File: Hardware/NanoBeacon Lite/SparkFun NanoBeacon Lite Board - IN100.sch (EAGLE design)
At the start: 34 parts, among them J3 Vertical Qwiic Connector, U1 IN100, Y1 CRYSTAL-26MHZSMD-3.2X2.5

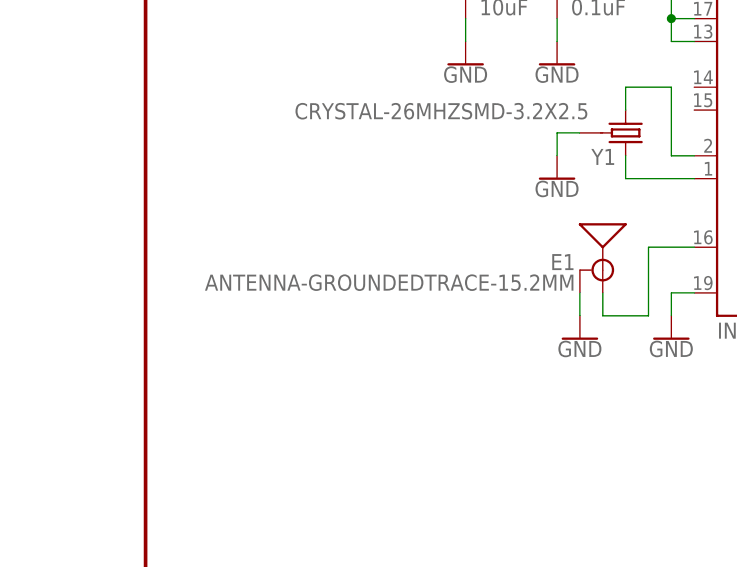
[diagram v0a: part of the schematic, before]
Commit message: Remove library file
Part is in SFE Eagle library, update part in design
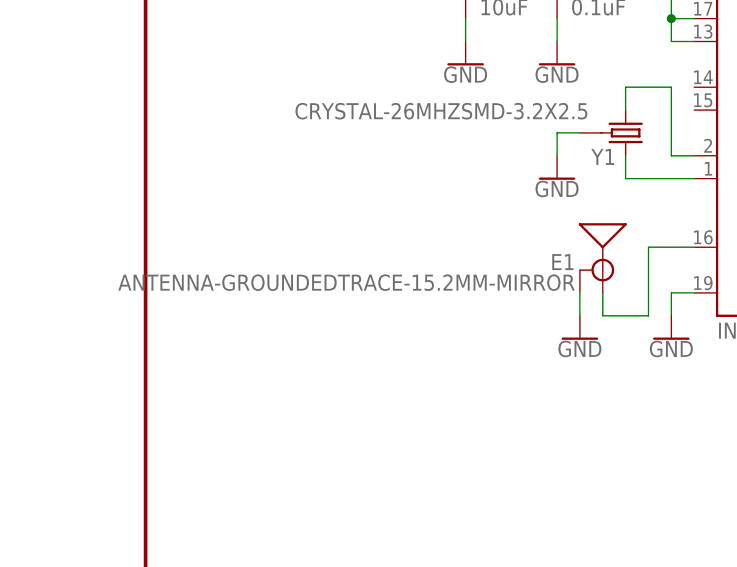
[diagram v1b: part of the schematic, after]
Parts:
- BT1: device SparkFun-Batteries:BATTERY-12MM_SMD -> SparkFun-Batteries:BATTERY-12MM_SMD_BOTH_PWR_PADS
- E1: value ANTENNA-GROUNDEDTRACE-15.2MM -> ANTENNA-GROUNDEDTRACE-15.2MM-MIRROR; device SparkFun-RF:ANTENNA-GROUNDEDTRACE-15.2MM -> SparkFun-RF:ANTENNA-GROUNDEDTRACE-15.2MM-MIRROR
- U1: device IN100:IN100 -> SparkFun-RF:IN100
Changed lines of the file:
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@@
 </classes>
 <parts>
-<part name="E1" library="SparkFun-RF" deviceset="ANTENNA-GROUNDED" device="TRACE-15.2MM"/>
+<part name="E1" library="SparkFun-RF" deviceset="ANTENNA-GROUNDED" device="TRACE-15.2MM-MIRROR" value="ANTENNA-GROUNDEDTRACE-15.2MM-MIRROR"/>
 <part name="FRAME1" library="SparkFun-Aesthetics" deviceset="FRAME-LETTER" device=""/>
-<part name="U1" library="IN100" deviceset="IN100" device=""/>
+<part name="U1" library="SparkFun-RF" deviceset="IN100" device=""/>
 <part name="GND1" library="SparkFun-PowerSymbols" deviceset="GND" device=""/>
 <part name="GND2" library="SparkFun-PowerSymbols" deviceset="GND" device=""/>
@@
 <part name="GND4" library="SparkFun-PowerSymbols" deviceset="GND" device=""/>
 <part name="J1" library="SparkFun-Connectors" deviceset="CONN_06" device="NO_SILK_NO_POP"/>
-<part name="BT1" library="SparkFun-Batteries" deviceset="BATTERY" device="-12MM_SMD"/>
+<part name="BT1" library="SparkFun-Batteries" deviceset="BATTERY" device="-12MM_SMD_BOTH_PWR_PADS"/>
 <part name="GND6" library="SparkFun-PowerSymbols" deviceset="GND" device=""/>
 <part name="H1" library="SparkFun-Hardware" deviceset="STAND-OFF" device=""/>
